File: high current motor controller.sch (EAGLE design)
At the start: 49 parts, among them IC1 LM2676S, Q1 IPT004N03L, Q2 IPT004N03L, Q3 IPT004N03L, Q4 IPT004N03L

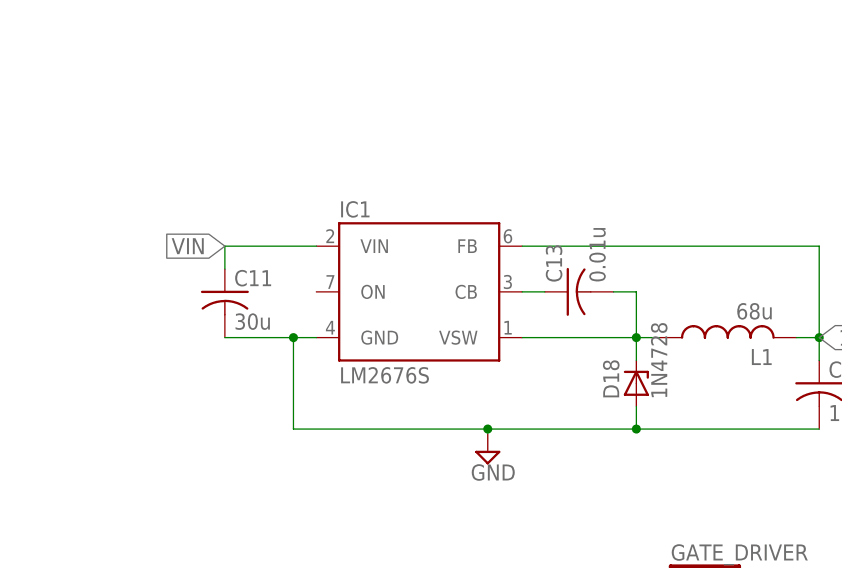
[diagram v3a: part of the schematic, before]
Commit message: Switching regulator components updated with correct values and packages
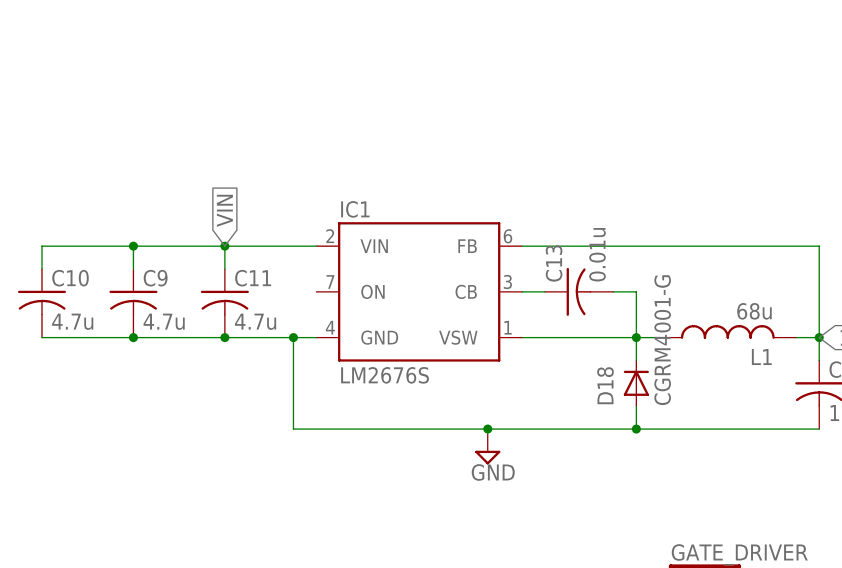
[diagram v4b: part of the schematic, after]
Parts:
- added C10, C9: 4.7u, resistor:C-USC0805
- C11: value 30u -> 4.7u
- D18: value 1N4728 -> CGRM4001-G; device diode:1N4728 -> diode:GF1
- L1: device resistor:L-USL1812 -> resistor:L-USWURTH12.8X12.8
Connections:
- net GND: now also C10.2, C9.2
- net VIN: now also C10.1, C9.1
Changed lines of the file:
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@@
 <grid distance="0.1" unitdist="inch" unit="inch" style="lines" multiple="1" display="no" altdistance="0.01" altunitdist="inch" altunit="inch"/>
 <layers>
-<layer number="1" name="Top" color="4" fill="11" visible="no" active="no"/>
+<layer number="1" name="Top" color="4" fill="1" visible="no" active="no"/>
 <layer number="16" name="Bottom" color="1" fill="1" visible="no" active="no"/>
 <layer number="17" name="Pads" color="2" fill="1" visible="no" active="no"/>
@@
 <layer number="49" name="Reference" color="7" fill="1" visible="no" active="no"/>
 <layer number="50" name="dxf" color="7" fill="1" visible="no" active="no"/>
-<layer number="51" name="tDocu" color="6" fill="1" visible="no" active="no"/>
+<layer number="51" name="tDocu" color="7" fill="1" visible="no" active="no"/>
 <layer number="52" name="bDocu" color="7" fill="1" visible="no" active="no"/>
 <layer number="53" name="tGND_GNDA" color="7" fill="9" visible="no" active="no"/>
@@
 <part name="BATT_POWER" library="pinhead" deviceset="PINHD-1X3" device=""/>
 <part name="IC1" library="v-reg-3" deviceset="LM2676" device="S"/>
-<part name="C11" library="resistor" deviceset="C-US" device="C0805" value="30u"/>
+<part name="C11" library="resistor" deviceset="C-US" device="C0805" value="4.7u"/>
 <part name="C12" library="resistor" deviceset="C-US" device="C0805" value="100u"/>
 <part name="C13" library="resistor" deviceset="C-US" device="C0805" value="0.01u"/>
-<part name="L1" library="resistor" deviceset="L-US" device="L1812" value="68u"/>
-<part name="D18" library="diode" deviceset="1N4728" device=""/>
+<part name="L1" library="resistor" deviceset="L-US" device="12.8X12.8" technology="WURTH" value="68u"/>
+<part name="D18" library="diode" deviceset="GF1" device="" value="CGRM4001-G"/>
 <part name="SUPPLY5" library="supply2" deviceset="GND" device=""/>
+<part name="C9" library="resistor" deviceset="C-US" device="C0805" value="4.7u"/>
+<part name="C10" library="resistor" deviceset="C-US" device="C0805" value="4.7u"/>
 </parts>
 <sheets>
@@
 <instance part="C13" gate="G$1" x="-35.56" y="38.1" rot="R90"/>
 <instance part="L1" gate="G$1" x="-17.78" y="33.02" rot="R90"/>
-<instance part="D18" gate="1" x="-27.94" y="27.94" rot="R90"/>
+<instance part="D18" gate="D" x="-27.94" y="27.94" rot="R90"/>
 <instance part="SUPPLY5" gate="GND" x="-44.45" y="20.32"/>
+<instance part="C9" gate="G$1" x="-83.82" y="38.1"/>
+<instance part="C10" gate="G$1" x="-93.98" y="38.1"/>
 </instances>
 <busses>
@@
 <wire x1="-66.04" y1="22.86" x2="-66.04" y2="33.02" width="0.1524" layer="91"/>
 <junction x="-66.04" y="33.02"/>
-<pinref part="D18" gate="1" pin="A"/>
+<pinref part="D18" gate="D" pin="A"/>
 <wire x1="-27.94" y1="25.4" x2="-27.94" y2="22.86" width="0.1524" layer="91"/>
 <junction x="-27.94" y="22.86"/>
 <pinref part="SUPPLY5" gate="GND" pin="GND"/>
 <junction x="-44.45" y="22.86"/>
+<pinref part="C9" gate="G$1" pin="2"/>
+<wire x1="-73.66" y1="33.02" x2="-83.82" y2="33.02" width="0.1524" layer="91"/>
+<junction x="-73.66" y="33.02"/>
+<pinref part="C10" gate="G$1" pin="2"/>
+<wire x1="-83.82" y1="33.02" x2="-93.98" y2="33.02" width="0.1524" layer="91"/>
+<junction x="-83.82" y="33.02"/>
 </segment>
 </net>
@@
 <wire x1="-63.5" y1="43.18" x2="-73.66" y2="43.18" width="0.1524" layer="91"/>
 <wire x1="-73.66" y1="43.18" x2="-73.66" y2="40.64" width="0.1524" layer="91"/>
-<label x="-73.66" y="43.18" size="1.778" layer="95" rot="R180" xref="yes"/>
+<label x="-73.66" y="43.18" size="1.778" layer="95" rot="R90" xref="yes"/>
+<pinref part="C10" gate="G$1" pin="1"/>
+<wire x1="-93.98" y1="40.64" x2="-93.98" y2="43.18" width="0.1524" layer="91"/>
+<wire x1="-93.98" y1="43.18" x2="-83.82" y2="43.18" width="0.1524" layer="91"/>
+<junction x="-73.66" y="43.18"/>
+<pinref part="C9" gate="G$1" pin="1"/>
+<wire x1="-83.82" y1="43.18" x2="-73.66" y2="43.18" width="0.1524" layer="91"/>
+<wire x1="-83.82" y1="40.64" x2="-83.82" y2="43.18" width="0.1524" layer="91"/>
+<junction x="-83.82" y="43.18"/>
 </segment>
 </net>
@@
 <pinref part="L1" gate="G$1" pin="1"/>
 <wire x1="-40.64" y1="33.02" x2="-27.94" y2="33.02" width="0.1524" layer="91"/>
-<pinref part="D18" gate="1" pin="C"/>
+<pinref part="D18" gate="D" pin="C"/>
 <wire x1="-27.94" y1="33.02" x2="-25.4" y2="33.02" width="0.1524" layer="91"/>
 <wire x1="-27.94" y1="30.48" x2="-27.94" y2="33.02" width="0.1524" layer="91"/>
